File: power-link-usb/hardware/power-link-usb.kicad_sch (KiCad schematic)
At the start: 30 parts, among them J1 KitProg3, J102 DX07S016JA3, J103 NE8FAH, J104 NE8FAH, Q101 BSC010N04LS, Q102 BSC010N04LS, U101 CYPM1311-48LDXI

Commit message: Refresh
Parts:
- INFO101: value ~ -> (none)

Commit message: Update
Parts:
- C101, C102, C103, C104, C105, C106, C107, C108: Id (none) -> Capacitor:${SYMBOL_NAME}
- D101: Id (none) -> LED:${SYMBOL_NAME}; Rating (none) -> 605nm
- D102: Id (none) -> LED:${SYMBOL_NAME}; Rating (none) -> 630nm
- J102: Id (none) -> USB:${SYMBOL_NAME}; Rating (none) -> USB2.0
- J103, J104: Id (none) -> EtherCon:${SYMBOL_NAME}
- Q101, Q102: Id (none) -> MOSFET:${SYMBOL_NAME}
- R101, R102, R103, R104, R105: Id (none) -> Resistor:${SYMBOL_NAME}
- TVS101, TVS102: Id (none) -> Diode:${SYMBOL_NAME}
- U101: Id (none) -> USB:${SYMBOL_NAME}; Rating (none) -> 28V
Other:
- moved on the sheet: C108, D102, FID101, FID102, ICON101, INFO101, INFO102, R101, R103, R105, TVS102

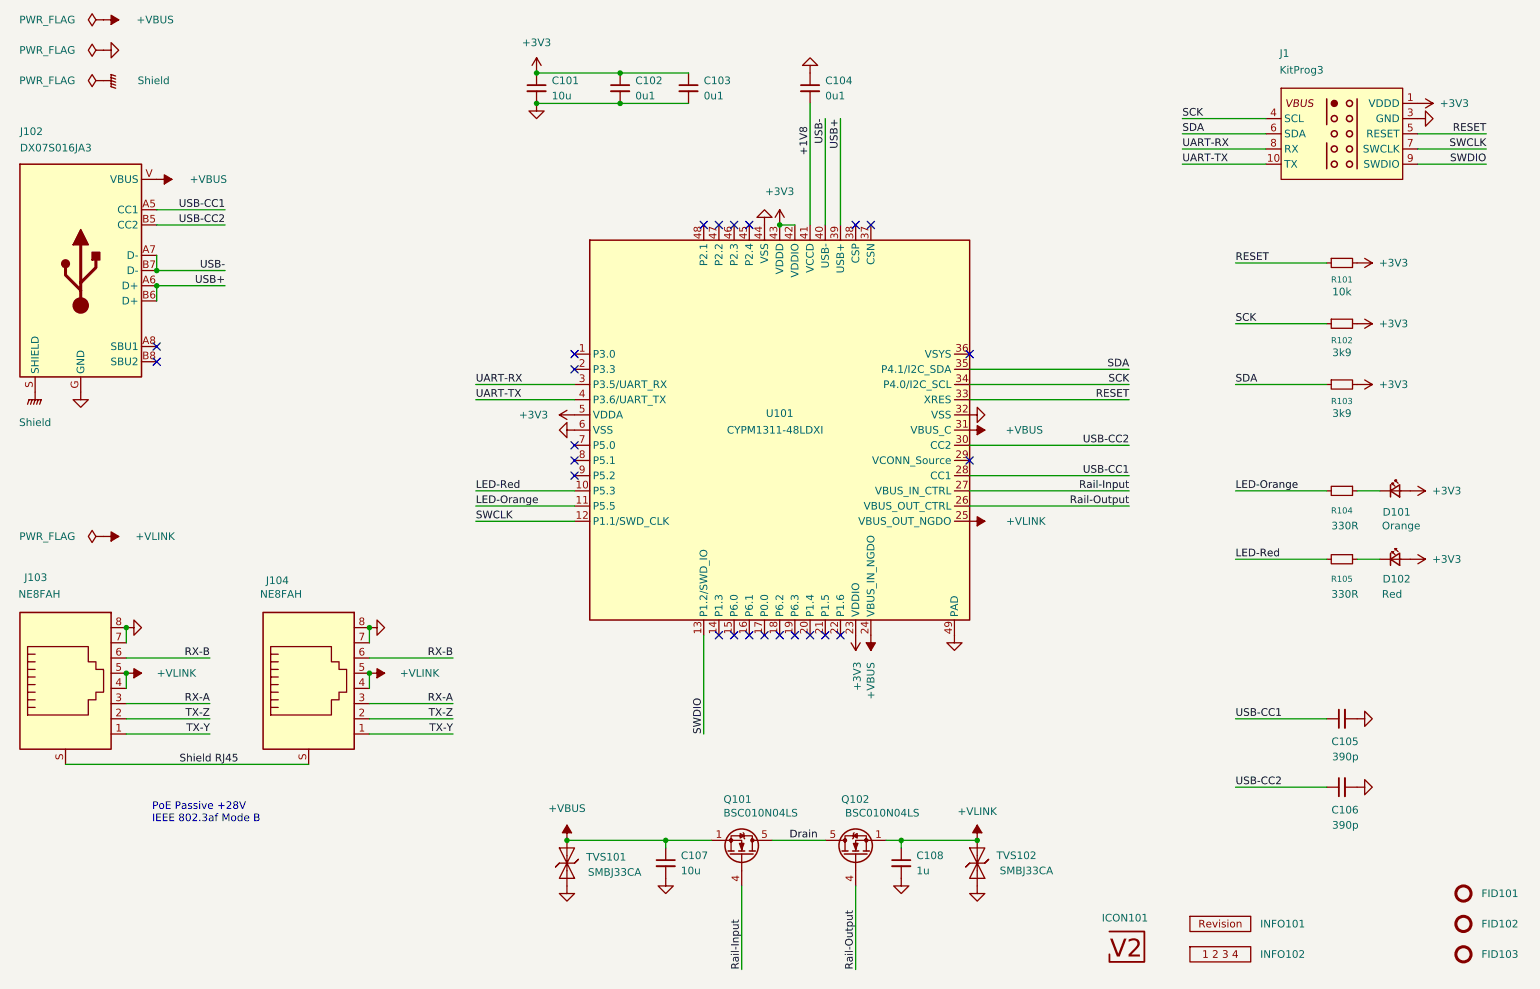
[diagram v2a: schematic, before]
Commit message: power-link-usb: split out PowerDelivery
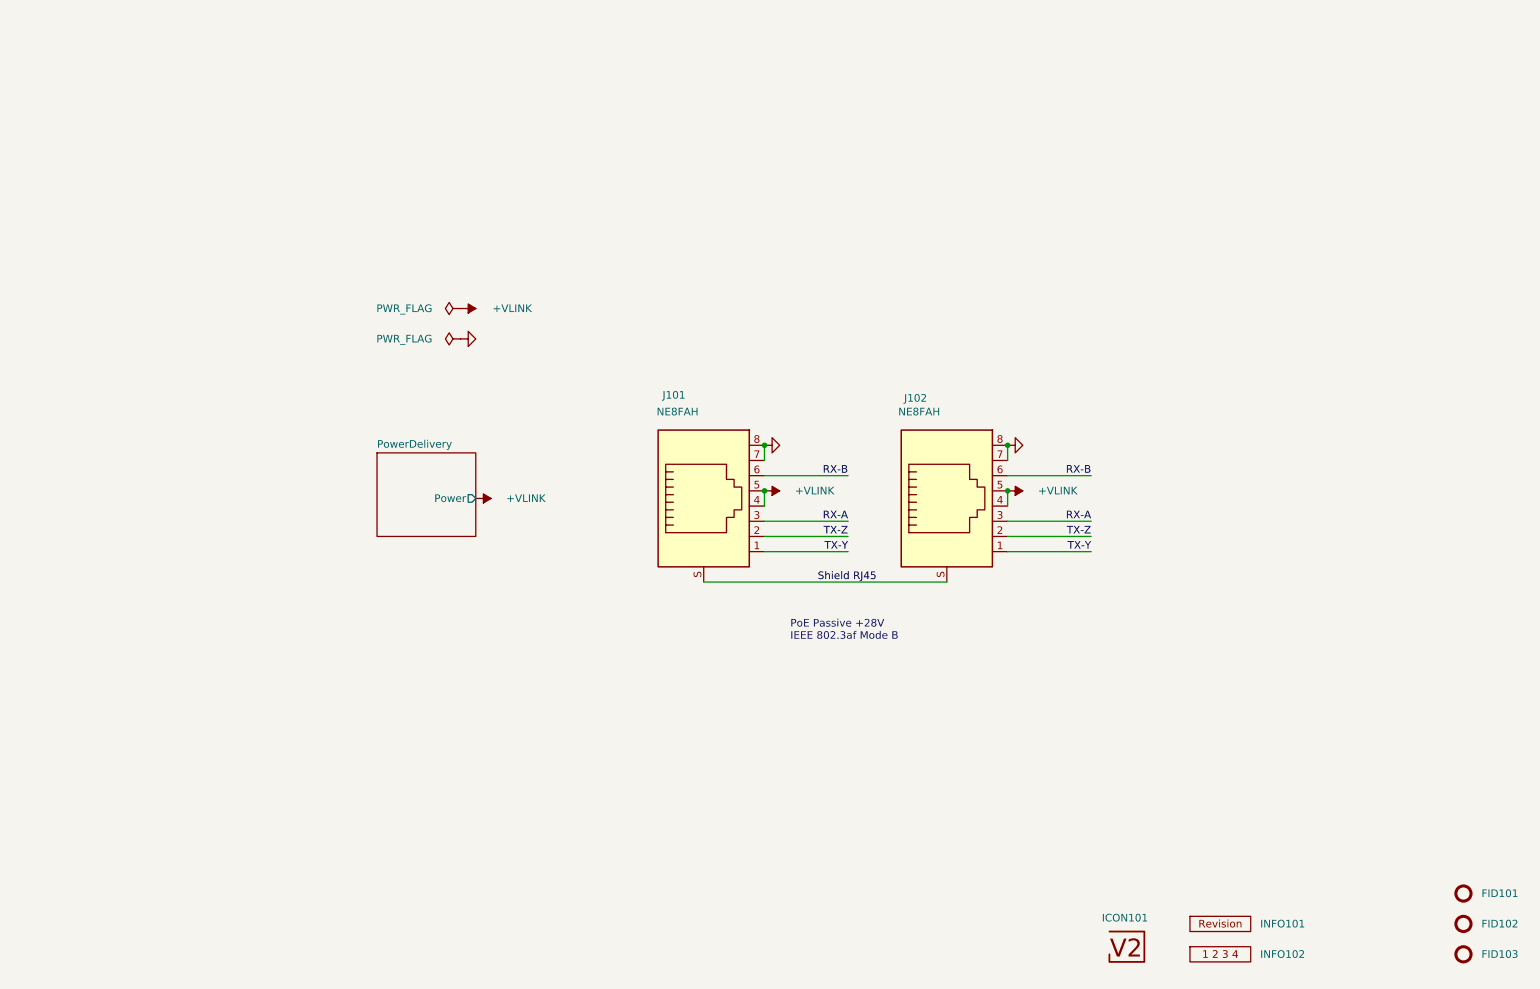
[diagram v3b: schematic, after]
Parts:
- removed C101: 10u, V2_Capacitor_SMD:C_0603, symbol V2_Capacitor:0603_10u
- removed C102, C103, C104: 0u1, V2_Capacitor_SMD:C_0603, symbol V2_Capacitor:0603_0u1
- removed C105, C106: 390p, V2_Capacitor_SMD:C_0603, symbol V2_Capacitor:0603_390p
- removed C107: 10u, V2_Capacitor_SMD:C_0805, symbol V2_Capacitor:0805_10u
- removed C108: 1u, V2_Capacitor_SMD:C_0603, symbol V2_Capacitor:0603_1u
- removed D101: Orange, V2_LED:LED_0603, symbol V2_LED:0603_Orange
- removed D102: Red, V2_LED:LED_0603, symbol V2_LED:0603_Red
- removed J1: KitProg3, V2_Connector_Debug:KitProg3, symbol V2_Connector_Debug:KitProg3
- removed J102: DX07S016JA3, V2_Connector_USB:JAE_DX07S016JA3, symbol V2_Connector_USB:JAE_DX07S016JA3
- removed Q101, Q102: BSC010N04LS, V2_Package_TO_SOT_SMD:TDSON-8-FL, symbol V2_Transistor_FET:BSC010N04LS
- removed R101: 10k, V2_Resistor_SMD:R_0603, symbol V2_Resistor:0603_10k
- removed R102, R103: 3k9, V2_Resistor_SMD:R_0603, symbol V2_Resistor:0603_3k9
- removed R104, R105: 330R, V2_Resistor_SMD:R_0603, symbol V2_Resistor:0603_330R
- removed TVS101, TVS102: SMBJ33CA, V2_Diode_SMD:D_SMB, symbol V2_Diode:SMBJ33CA
- removed U101: CYPM1311-48LDXI, V2_Package_DFN_QFN:QFN-48-1EP_6x6mm_P0.4mm_EP4.6x4.6mm, symbol V2_Interface_USB:CYPM1311-48LDXI
- J101: renamed from J103; Rating (none) -> CAT5e
- J102: renamed from J104; Rating (none) -> CAT5e
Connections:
- no-connect marks 24 -> 0
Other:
- added sheet PowerDelivery (PowerDelivery.kicad_sch)
- moved on the sheet: J101, J102

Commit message: Update
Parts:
- added TVS101: SMBJ33CA, V2_Diode_SMD:D_SMB, symbol V2_Diode:SMBJ33CA
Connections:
- net +VLINK: now also TVS101.2 (A)
- net GND: now also TVS101.1 (K)
- no-connect marks 0 -> 2
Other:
- sheet PowerDelivery ports: added UART-RX, UART-TX; removed none
